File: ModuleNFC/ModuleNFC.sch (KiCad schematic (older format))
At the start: 40 parts, among them J1 Conn_01x10_Male, J2 Conn_01x04_Male, J3 Conn_01x08_Male, J4 Conn_Coaxial, Q1 2N7002DM, SW1 SW_DIP_x02, U1 PN5321A3HN_C1xx, Y1 27.12MHz

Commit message: Esquemático y PCB versión 1
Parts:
- Y1: footprint Crystal:Crystal_SMD_0603-4Pin_6.0x3.5mm -> Crystal:Crystal_SMD_0603-2Pin_6.0x3.5mm
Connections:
- net +3V3: now also J3.5 (Pin_5); no longer J3.4 (Pin_4)
- net GND: now also J3.6 (Pin_6); no longer J3.3 (Pin_3)
- net RSTOUTN: now also J3.8 (Pin_8); no longer J3.1 (Pin_1)
- net at J3.2 (Pin_2): now also R9.1; no longer R12.1
- net at R11.1: now also J3.4 (Pin_4); no longer J3.5 (Pin_5)
- net at R10.1: now also J3.3 (Pin_3); no longer J3.6 (Pin_6)
- net at J3.7 (Pin_7): now also R12.1; no longer R9.1
- net at R8.1: now also J3.1 (Pin_1); no longer J3.8 (Pin_8)
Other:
- moved on the sheet: R10, R11, R12, R8, R9
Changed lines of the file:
@@
 F 0 "Y1" H 4275 4200 50  0000 R CNN
 F 1 "27.12MHz" H 4425 4500 50  0000 R CNN
-F 2 "Crystal:Crystal_SMD_0603-4Pin_6.0x3.5mm" H 4225 4350 50  0001 C CNN
+F 2 "Crystal:Crystal_SMD_0603-2Pin_6.0x3.5mm" H 4225 4350 50  0001 C CNN
 F 3 "~" H 4225 4350 50  0001 C CNN
 	1    4225 4350
@@
 L Device:R R8
 U 1 1 5F90C42F
-P 9750 1425
-F 0 "R8" V 9700 1600 50  0000 C CNN
-F 1 "100" V 9800 1625 50  0000 C CNN
-F 2 "Resistor_SMD:R_0402_1005Metric" V 9680 1425 50  0001 C CNN
-F 3 "~" H 9750 1425 50  0001 C CNN
-	1    9750 1425
+P 9750 2125
+F 0 "R8" V 9700 2300 50  0000 C CNN
+F 1 "100" V 9800 2325 50  0000 C CNN
+F 2 "Resistor_SMD:R_0402_1005Metric" V 9680 2125 50  0001 C CNN
+F 3 "~" H 9750 2125 50  0001 C CNN
+	1    9750 2125
 	0    1    1    0
 $EndComp
-Wire Wire Line
-	10450 1425 9900 1425
 Text Label 4750 3325 2    50   ~ 0
 SCK
-Text Label 9250 1425 2    50   ~ 0
+Text Label 9250 2125 2    50   ~ 0
 SCK
-Wire Wire Line
-	9600 1425 9250 1425
 Wire Wire Line
 	4875 3325 4750 3325
@@
 L Device:R R9
 U 1 1 5F92D551
-P 10175 1525
-F 0 "R9" V 10125 1725 50  0000 C CNN
-F 1 "100" V 10225 1725 50  0000 C CNN
-F 2 "Resistor_SMD:R_0402_1005Metric" V 10105 1525 50  0001 C CNN
-F 3 "~" H 10175 1525 50  0001 C CNN
-	1    10175 1525
+P 10175 2025
+F 0 "R9" V 10125 2225 50  0000 C CNN
+F 1 "100" V 10225 2225 50  0000 C CNN
+F 2 "Resistor_SMD:R_0402_1005Metric" V 10105 2025 50  0001 C CNN
+F 3 "~" H 10175 2025 50  0001 C CNN
+	1    10175 2025
 	0    1    1    0
 $EndComp
-Wire Wire Line
-	10450 1525 10325 1525
-Text Label 9250 1525 2    50   ~ 0
+Text Label 9250 2025 2    50   ~ 0
 MISO
 Text Label 4750 3225 2    50   ~ 0
@@
 Wire Wire Line
 	4750 3225 4875 3225
-Wire Wire Line
-	10025 1525 9250 1525
 $Comp
 L Device:R R10
 U 1 1 5F947337
-P 9750 1625
-F 0 "R10" V 9700 1425 50  0000 C CNN
-F 1 "100" V 9800 1425 50  0000 C CNN
-F 2 "Resistor_SMD:R_0402_1005Metric" V 9680 1625 50  0001 C CNN
-F 3 "~" H 9750 1625 50  0001 C CNN
-	1    9750 1625
+P 9750 1925
+F 0 "R10" V 9700 1725 50  0000 C CNN
+F 1 "100" V 9800 1725 50  0000 C CNN
+F 2 "Resistor_SMD:R_0402_1005Metric" V 9680 1925 50  0001 C CNN
+F 3 "~" H 9750 1925 50  0001 C CNN
+	1    9750 1925
 	0    1    1    0
 $EndComp
-Wire Wire Line
-	10450 1625 9900 1625
-Text Label 9250 1625 2    50   ~ 0
+Text Label 9250 1925 2    50   ~ 0
 MOSI_SDA_TX
-Wire Wire Line
-	9600 1625 9250 1625
 $Comp
 L Device:R R11
 U 1 1 5F95B600
-P 10175 1725
-F 0 "R11" V 10125 1550 50  0000 C CNN
-F 1 "100" V 10225 1525 50  0000 C CNN
-F 2 "Resistor_SMD:R_0402_1005Metric" V 10105 1725 50  0001 C CNN
-F 3 "~" H 10175 1725 50  0001 C CNN
-	1    10175 1725
+P 10175 1825
+F 0 "R11" V 10125 1650 50  0000 C CNN
+F 1 "100" V 10225 1625 50  0000 C CNN
+F 2 "Resistor_SMD:R_0402_1005Metric" V 10105 1825 50  0001 C CNN
+F 3 "~" H 10175 1825 50  0001 C CNN
+	1    10175 1825
 	0    1    1    0
 $EndComp
-Wire Wire Line
-	10450 1725 10325 1725
-Text Label 9250 1725 2    50   ~ 0
+Text Label 9250 1825 2    50   ~ 0
 NSS_SCL_RX
-Wire Wire Line
-	10025 1725 9250 1725
 $Comp
 L power:+3.3V #PWR0123
@@
 	1    0    0    -1
 $EndComp
-Text Label 9250 1825 2    50   ~ 0
+Text Label 9250 1725 2    50   ~ 0
 Vcc
 Text Label 9825 3225 2    50   ~ 0
@@
 Wire Wire Line
 	9825 2925 9825 3075
-Text Label 9250 1925 2    50   ~ 0
+Text Label 9250 1625 2    50   ~ 0
 Masa
-Wire Wire Line
-	10450 1825 9250 1825
-Wire Wire Line
-	10450 1925 9250 1925
-Text Label 9250 2025 2    50   ~ 0
+Text Label 9250 1525 2    50   ~ 0
 IRQ
 $Comp
 L Device:R R12
 U 1 1 5F9D8B35
-P 9750 2025
-F 0 "R12" V 9700 1850 50  0000 C CNN
-F 1 "100" V 9800 1825 50  0000 C CNN
-F 2 "Resistor_SMD:R_0402_1005Metric" V 9680 2025 50  0001 C CNN
-F 3 "~" H 9750 2025 50  0001 C CNN
-	1    9750 2025
+P 9750 1525
+F 0 "R12" V 9700 1350 50  0000 C CNN
+F 1 "100" V 9800 1325 50  0000 C CNN
+F 2 "Resistor_SMD:R_0402_1005Metric" V 9680 1525 50  0001 C CNN
+F 3 "~" H 9750 1525 50  0001 C CNN
+	1    9750 1525
 	0    1    1    0
 $EndComp
-Wire Wire Line
-	9250 2025 9600 2025
-Wire Wire Line
-	9900 2025 10450 2025
 Text Label 4750 2825 2    50   ~ 0
 IRQ
@@
 Wire Wire Line
 	4875 2725 4750 2725
-Text Label 9250 2125 2    50   ~ 0
+Text Label 9250 1425 2    50   ~ 0
 RSTOUTN
-Wire Wire Line
-	10450 2125 9250 2125
 Wire Wire Line
 	8400 4950 8175 4950
@@
 Text Notes 9575 1125 0    55   ~ 11
 Señales de SPI
+Wire Wire Line
+	10450 2125 9900 2125
+Wire Wire Line
+	9600 2125 9250 2125
+Wire Wire Line
+	10450 1425 9250 1425
+Wire Wire Line
+	10450 2025 10325 2025
+Wire Wire Line
+	10025 2025 9250 2025
+Wire Wire Line
+	9900 1525 10450 1525
+Wire Wire Line
+	9600 1525 9250 1525
+Wire Wire Line
+	10450 1925 9900 1925
+Wire Wire Line
+	9600 1925 9250 1925
+Wire Wire Line
+	10450 1625 9250 1625
+Wire Wire Line
+	10450 1725 9250 1725
+Wire Wire Line
+	10325 1825 10450 1825
+Wire Wire Line
+	10025 1825 9250 1825
 $EndSCHEMATC

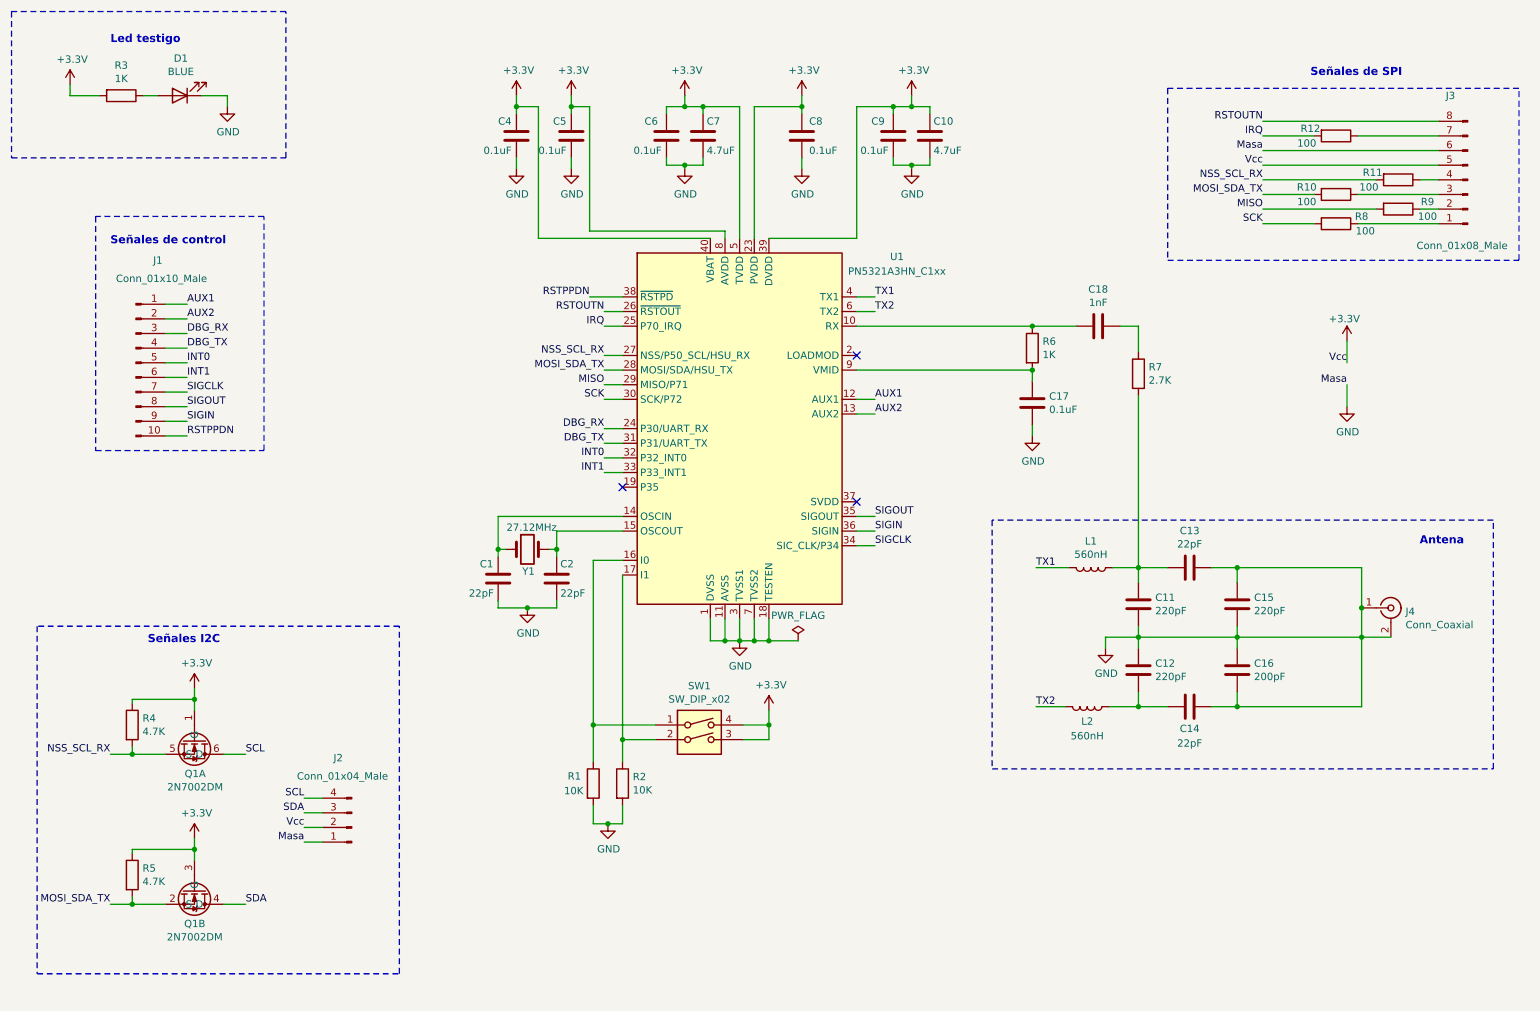
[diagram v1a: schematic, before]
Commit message: Add model 3D of PN532
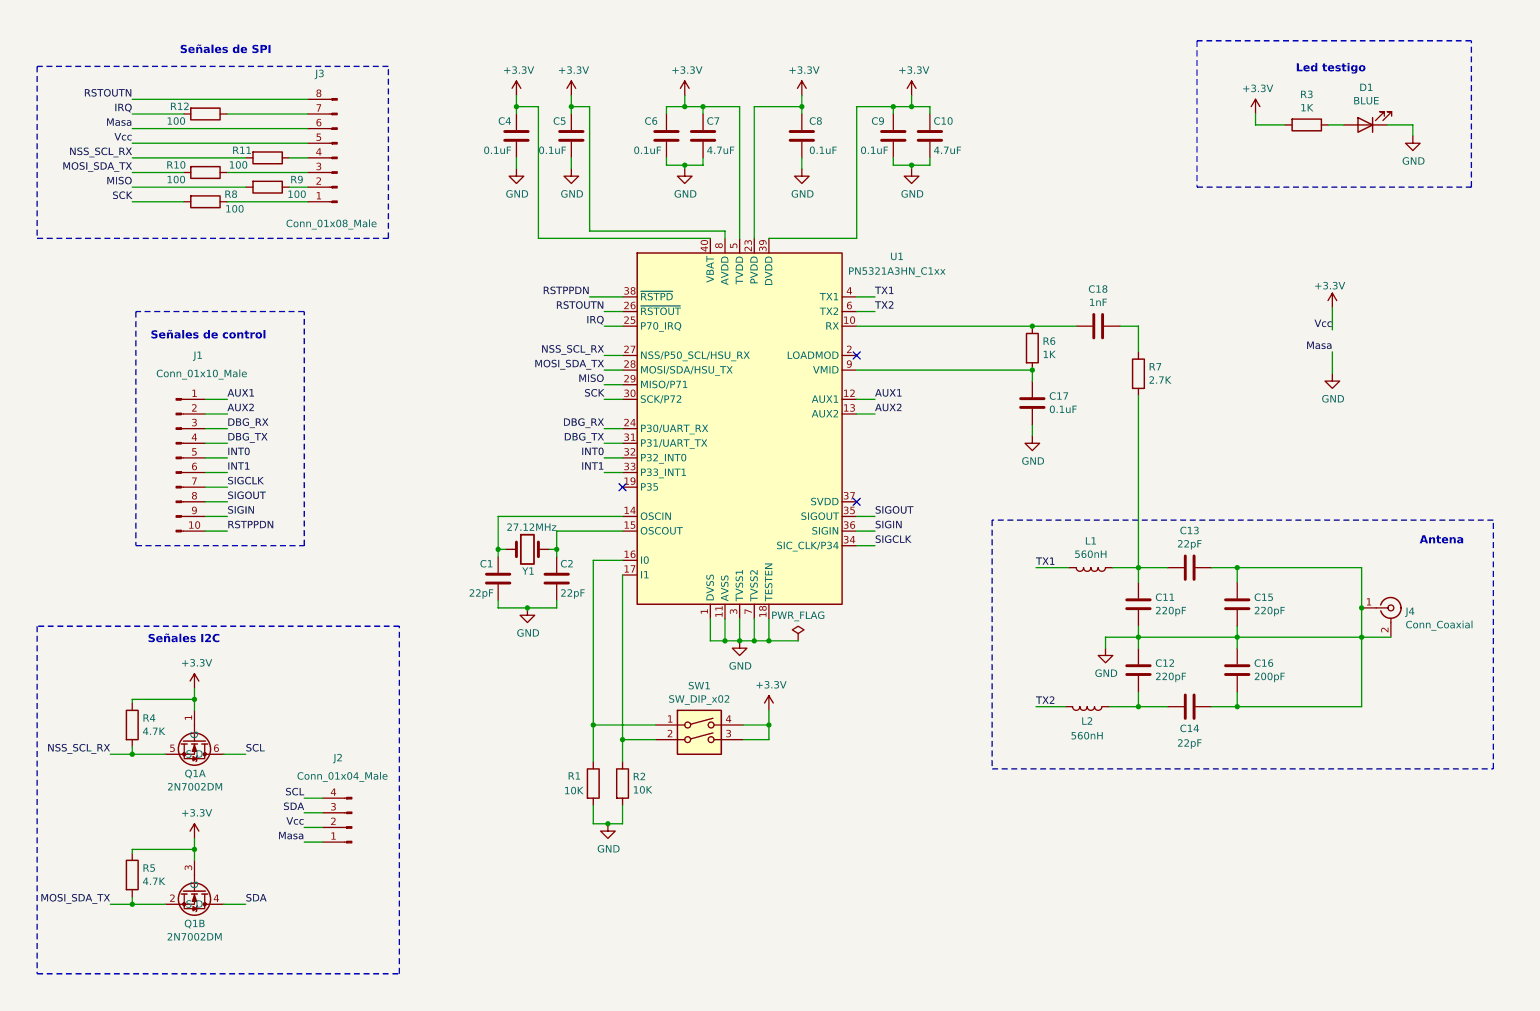
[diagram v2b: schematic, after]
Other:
- moved on the sheet: D1, J1, J3, R10, R11, R12, R3, R8, R9

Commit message: Modification on PCB and Schematic on base of correction
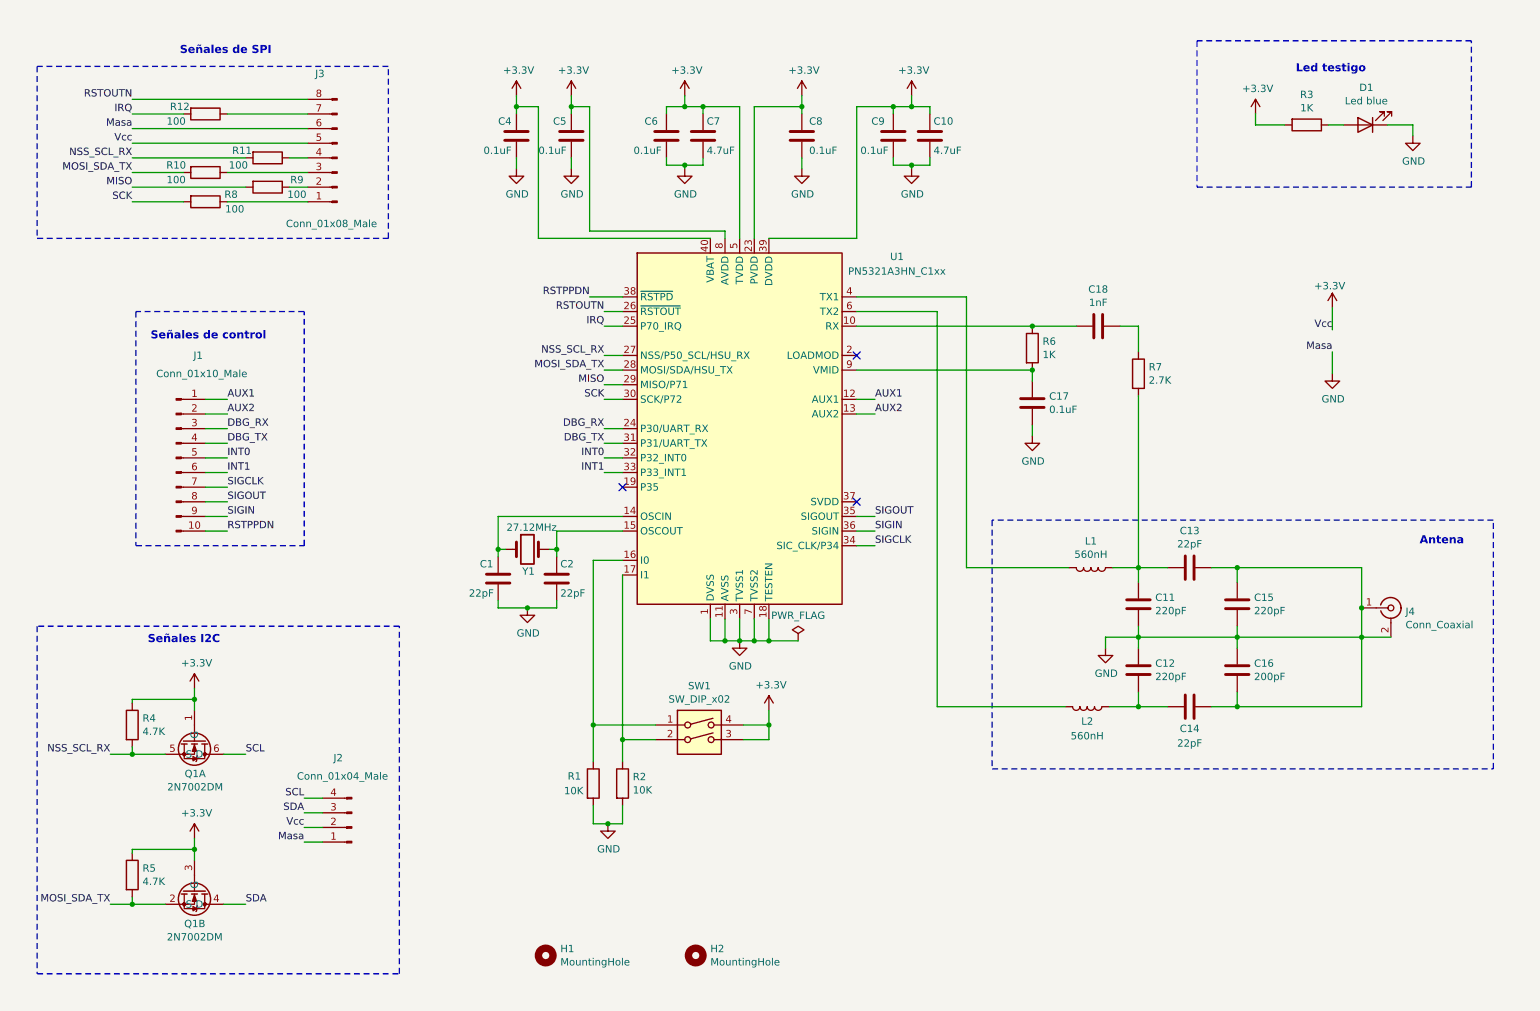
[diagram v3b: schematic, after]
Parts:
- added H1, H2: MountingHole, MountingHole:MountingHole_2.2mm_M2_Pad_Via, symbol Mechanical:MountingHole
- D1: value BLUE -> Led blue
- J4: Part Number (none) -> 538-73412-0110; Supplier (none) -> MOUSER
- SW1: footprint Button_Switch_SMD:SW_DIP_SPSTx02_Slide_6.7x6.64mm_W8.61mm_P2.54mm_LowProfile -> Button_Switch_SMD:SW_DIP_SPSTx02_Slide_KingTek_DSHP02TS_W7.62mm_P1.27mm; Part Number (none) -> CT3108CT-ND; Supplier (none) -> Digi-key
- U1: Part Number (none) -> 568-13228-ND; Supplier (none) -> Digi-key
- Y1: Part Number (none) -> XC1671TR-ND; Supplier (none) -> Digi-key
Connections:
- net TX1: no longer names the net of L1.2, U1.4 (TX1)
- net TX2: no longer names the net of L2.2, U1.6 (TX2)
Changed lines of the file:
@@
 encoding utf-8
 Sheet 1 1
-Title "ModuloNFC"
+Title "Módulo NFC"
 Date "2020-09-25"
 Rev "v1"
 Comp "Hanes Nahuel Sciarrone"
-Comment1 ""
+Comment1 "Licencia BSD"
 Comment2 ""
 Comment3 ""
@@
 F 1 "27.12MHz" H 4425 4500 50  0000 R CNN
 F 2 "Crystal:Crystal_SMD_0603-2Pin_6.0x3.5mm" H 4225 4350 50  0001 C CNN
-F 3 "~" H 4225 4350 50  0001 C CNN
+F 3 "https://ecsxtal.com/store/pdf/ecx-64a_ecx-64cr.pdf" H 4225 4350 50  0001 C CNN
+F 4 "XC1671TR-ND" H 4225 4350 50  0001 C CNN "Part Number"
+F 5 "Digi-key" H 4225 4350 50  0001 C CNN "Supplier"
 	1    4225 4350
 	1    0    0    -1
@@
 F 2 "RF_NFC_PN532:HVQFN-40-1EP_6x6mm_P0.5mm_EP4.1x4.1mm" H 7175 2275 50  0001 C CNN
 F 3 "https://www.nxp.com/docs/en/nxp/data-sheets/PN532_C1.pdf" H 5675 3725 50  0001 C CNN
+F 4 "Digi-key" H 5675 3525 50  0001 C CNN "Supplier"
+F 5 "568-13228-ND" H 5675 3525 50  0001 C CNN "Part Number"
 	1    5675 3525
 	1    0    0    -1
@@
 P 9950 1450
 F 0 "D1" H 9943 1195 50  0000 C CNN
-F 1 "BLUE" H 9943 1286 50  0000 C CNN
+F 1 "Led blue" H 9943 1286 50  0000 C CNN
 F 2 "LED_SMD:LED_0402_1005Metric" H 9950 1450 50  0001 C CNN
 F 3 "~" H 9950 1450 50  0001 C CNN
@@
 F 0 "SW1" H 5400 6017 50  0000 C CNN
 F 1 "SW_DIP_x02" H 5400 5926 50  0000 C CNN
-F 2 "Button_Switch_SMD:SW_DIP_SPSTx02_Slide_6.7x6.64mm_W8.61mm_P2.54mm_LowProfile" H 5400 5650 50  0001 C CNN
-F 3 "~" H 5400 5650 50  0001 C CNN
+F 2 "Button_Switch_SMD:SW_DIP_SPSTx02_Slide_KingTek_DSHP02TS_W7.62mm_P1.27mm" H 5400 5650 50  0001 C CNN
+F 3 "https://www.ctscorp.com/wp-content/uploads/218.pdf" H 5400 5650 50  0001 C CNN
+F 4 "Digi-key" H 5400 5650 50  0001 C CNN "Supplier"
+F 5 "CT3108CT-ND" H 5400 5650 50  0001 C CNN "Part Number"
 	1    5400 5650
 	1    0    0    -1
@@
 Wire Wire Line
 	9075 5425 8900 5425
-Text Label 7700 4475 0    50   ~ 0
-TX1
-Text Label 6600 2625 0    50   ~ 0
-TX1
-Text Label 6600 2725 0    50   ~ 0
-TX2
-Text Label 7700 5425 0    50   ~ 0
-TX2
-Wire Wire Line
-	7925 4475 7700 4475
-Wire Wire Line
-	7900 5425 7700 5425
-Wire Wire Line
-	6600 2625 6475 2625
-Wire Wire Line
-	6600 2725 6475 2725
 $Comp
 L Connector:Conn_01x10_Male J1
@@
 F 1 "Conn_Coaxial" H 10225 4634 50  0000 L CNN
 F 2 "Antena:U.FL_Molex_MCRF_73412-0110_Vertical" H 10125 4750 50  0001 C CNN
-F 3 " ~" H 10125 4750 50  0001 C CNN
+F 3 "https://ar.mouser.com/datasheet/2/276/1/0734120110_RF_COAX_CONNECTORS-173239.pdf" H 10125 4750 50  0001 C CNN
+F 4 "538-73412-0110 " H 10125 4750 50  0001 C CNN "Part Number"
+F 5 "MOUSER" H 10125 4750 50  0001 C CNN "Supplier"
 	1    10125 4750
 	1    0    0    -1
@@
 F 1 "2N7002DM" V 2224 6727 50  0000 C CNN
 F 2 "Package_SO:SC-74-6_1.5x2.9mm_P0.95mm" H 1950 6725 50  0001 C CNN
-F 3 "" H 1950 6725 50  0001 C CNN
+F 3 "https://pdf1.alldatasheet.com/datasheet-pdf/view/508035/LRC/L2N7002DMT1G.html" H 1950 6725 50  0001 C CNN
 	2    1950 6725
 	0    1    1    0
@@
 F 1 "2N7002DM" V 2224 5705 50  0000 C CNN
 F 2 "Package_SO:SC-74-6_1.5x2.9mm_P0.95mm" H 1950 5700 50  0001 C CNN
-F 3 "" H 1950 5700 50  0001 C CNN
+F 3 "https://pdf1.alldatasheet.com/datasheet-pdf/view/508035/LRC/L2N7002DMT1G.html" H 1950 5700 50  0001 C CNN
 	1    1950 5700
 	0    1    1    0
@@
 Wire Wire Line
 	2300 1675 1525 1675
+$Comp
+L Mechanical:MountingHole H1
+U 1 1 5F8296EC
+P 4350 7125
+F 0 "H1" H 4450 7171 50  0000 L CNN
+F 1 "MountingHole" H 4450 7080 50  0000 L CNN
+F 2 "MountingHole:MountingHole_2.2mm_M2_Pad_Via" H 4350 7125 50  0001 C CNN
+F 3 "~" H 4350 7125 50  0001 C CNN
+	1    4350 7125
+	1    0    0    -1
+$EndComp
+$Comp
+L Mechanical:MountingHole H2
+U 1 1 5F829A1D
+P 5375 7125
+F 0 "H2" H 5475 7171 50  0000 L CNN
+F 1 "MountingHole" H 5475 7080 50  0000 L CNN
+F 2 "MountingHole:MountingHole_2.2mm_M2_Pad_Via" H 5375 7125 50  0001 C CNN
+F 3 "~" H 5375 7125 50  0001 C CNN
+	1    5375 7125
+	1    0    0    -1
+$EndComp
+Wire Wire Line
+	6475 2625 7225 2625
+Wire Wire Line
+	7225 2625 7225 4475
+Wire Wire Line
+	7225 4475 7925 4475
+Wire Wire Line
+	6475 2725 7025 2725
+Wire Wire Line
+	7025 2725 7025 5425
+Wire Wire Line
+	7025 5425 7900 5425
 $EndSCHEMATC

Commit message: All modification with correction
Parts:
- added FID1, FID2, FID3: Fiducial, Fiducial:Fiducial_1mm_Mask2mm, symbol Mechanical:Fiducial
- C1, C10, C11, C12, C13, C14, C15, C16, C17, C18, C2, C4, C5, C6, C7, C8, C9: footprint Capacitor_SMD:C_0603_1608Metric -> Capacitor_SMD:C_0805_2012Metric
- D1: footprint LED_SMD:LED_0402_1005Metric -> LED_SMD:LED_0603_1608Metric
- R1, R2, R3, R4, R5, R6, R7: footprint Resistor_SMD:R_0603_1608Metric -> Resistor_SMD:R_0805_2012Metric
- R10, R11, R12, R8, R9: footprint Resistor_SMD:R_0402_1005Metric -> Resistor_SMD:R_0805_2012Metric
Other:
- moved on the sheet: H1, H2
